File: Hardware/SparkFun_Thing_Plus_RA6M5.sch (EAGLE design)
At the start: 91 parts, among them J1 USB Female Type C Connector, J2 THING_PLUS_LOGICAL, J3 QWIIC_RA, J4 CONN_03X2, J7 MICRO-SDFRICTION, Q2 20V/4.2A/52mΩ/1.4W, U1 R7FA6M5, U2 DA14531MOD, U3 MCP73831, U4 RT9080-33GJ5, U5 W25QXX128MBIT-6X5, U6 MCP1501-3.3V, U7 MAX17048, U8 LM66200, Y1 24.000MHz, Y2 32.768kHz

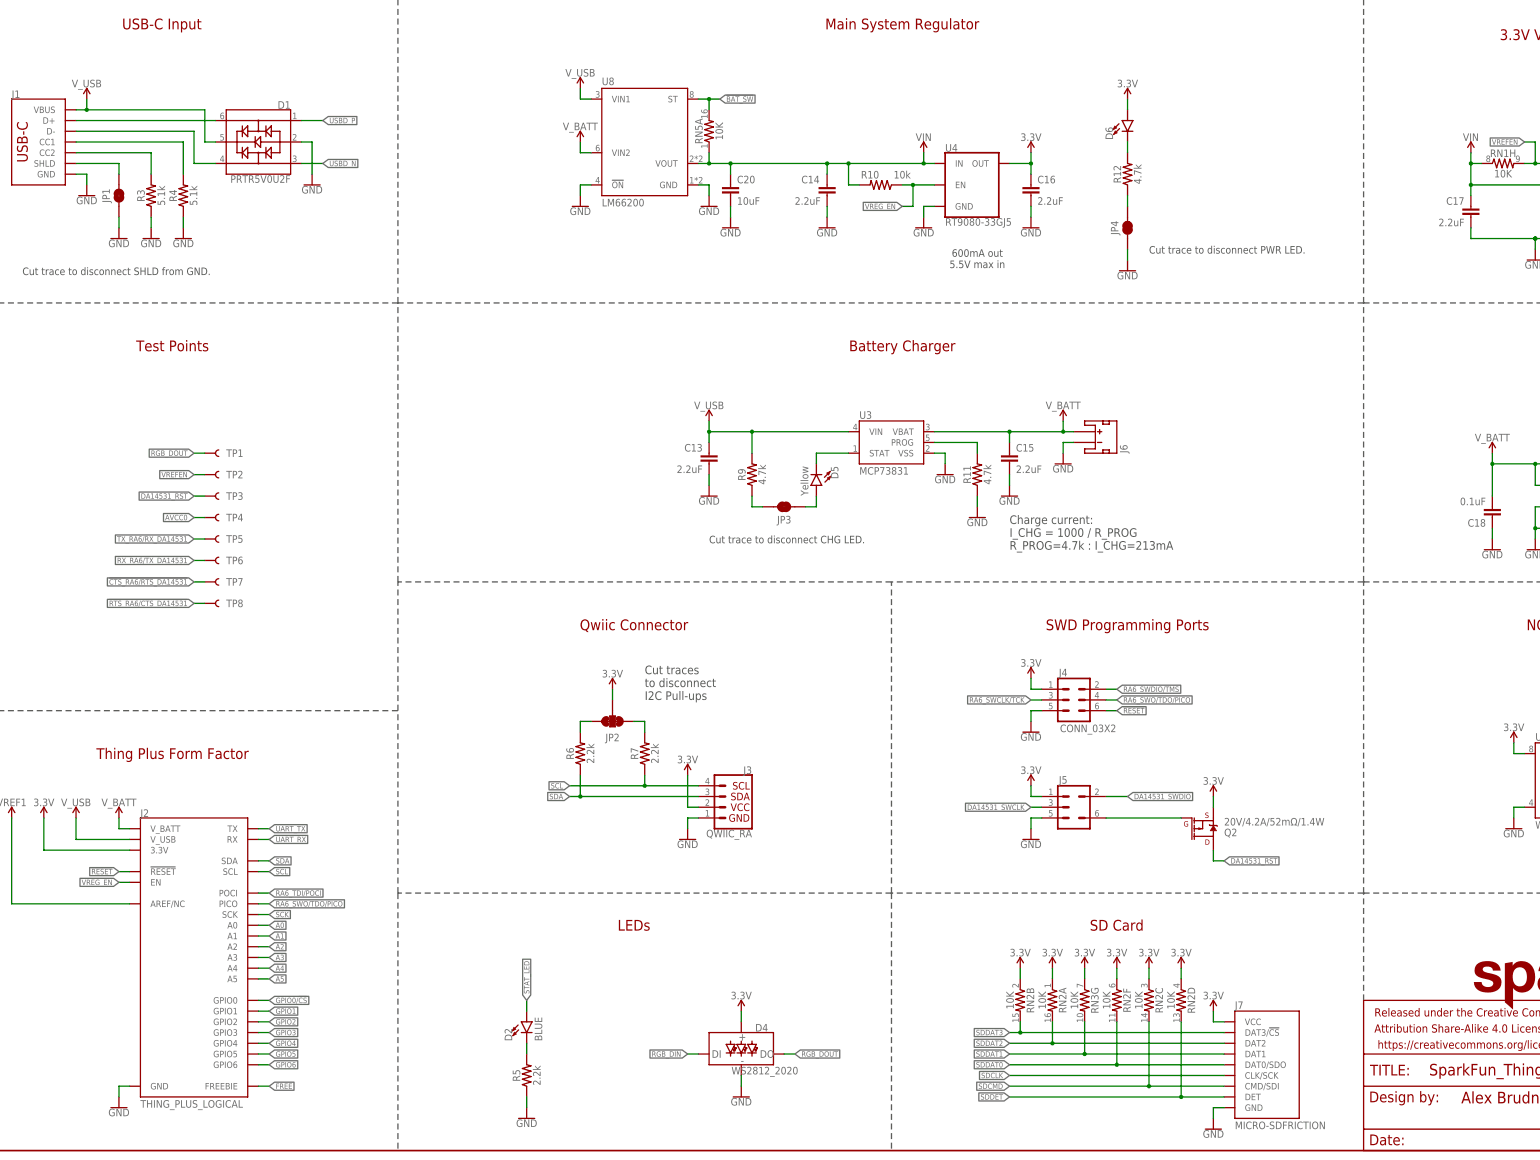
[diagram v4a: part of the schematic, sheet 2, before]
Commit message: update based on pre-design review comments.
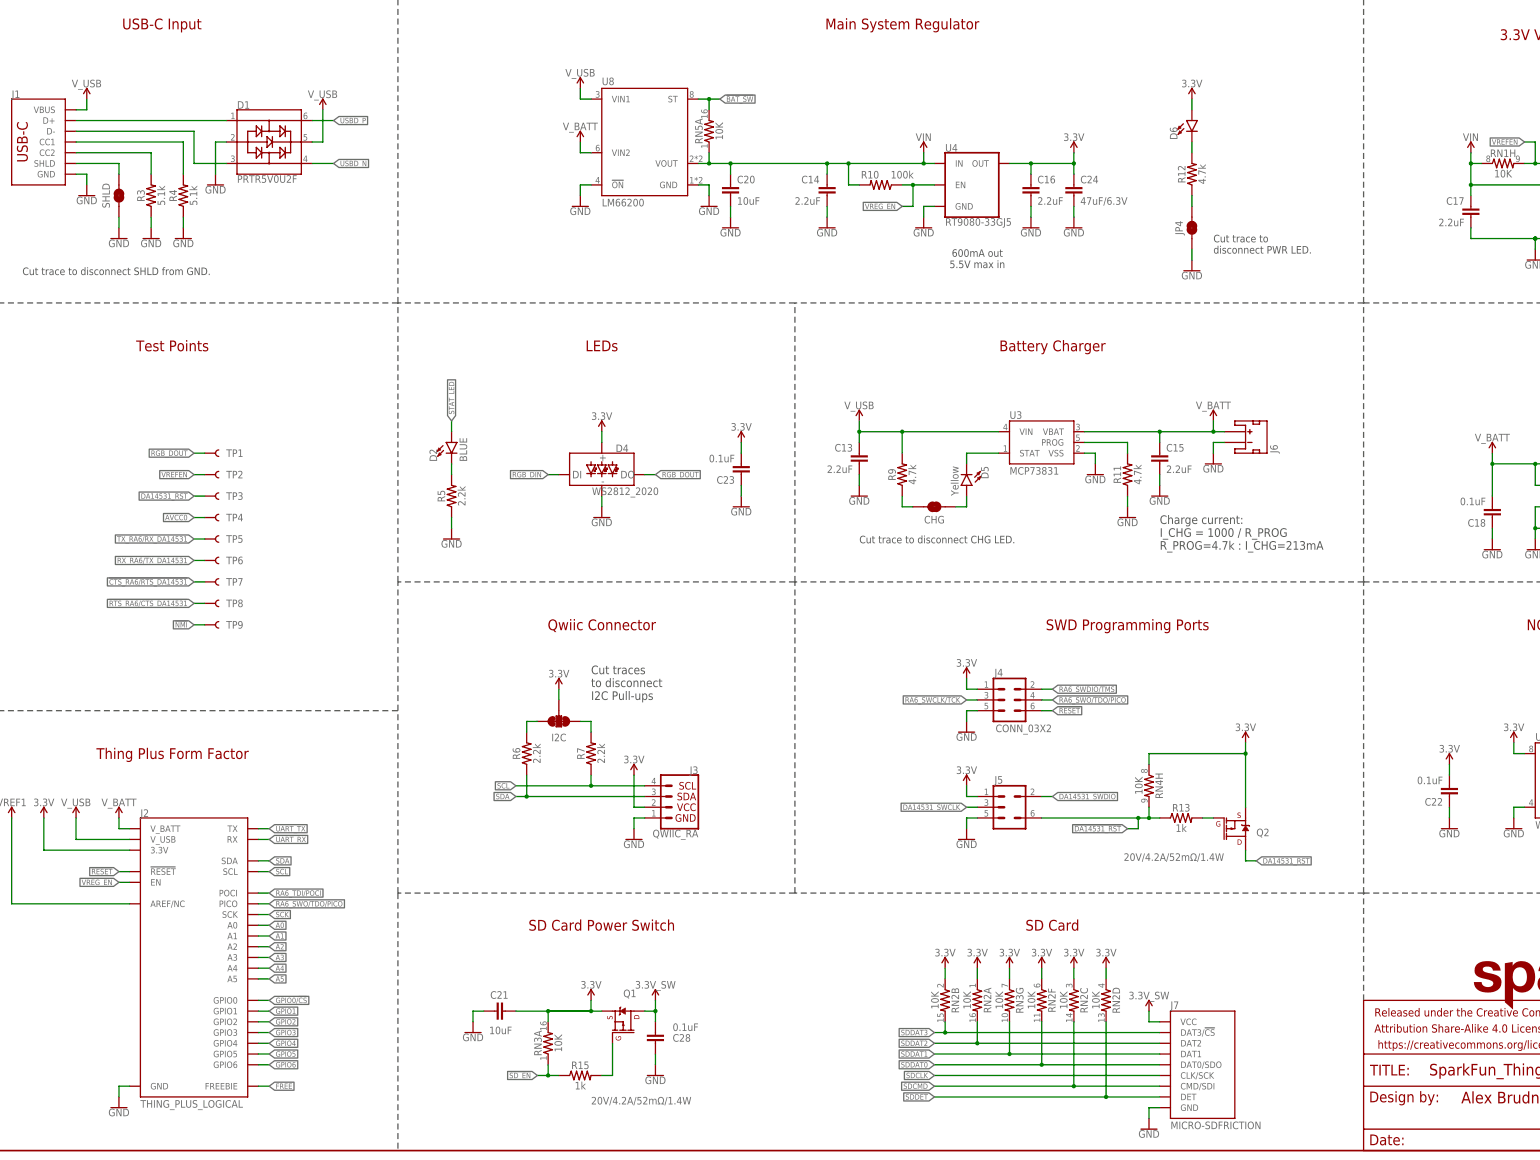
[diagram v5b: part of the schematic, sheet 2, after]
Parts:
- removed JP2: JUMPER-SMT_3_2-NC_TRACE_SILK, SparkFun-Jumpers:JUMPER-SMT_3_2-NC_TRACE_SILK
- removed JP3: JUMPER-SMT_2_NC_TRACE_SILK, SparkFun-Jumpers:JUMPER-SMT_2_NC_TRACE_SILK
- added C21: 10uF, SparkFun-Capacitors:10UF-0805-25V-10%
- added C22, C23, C28: 0.1uF, SparkFun-Capacitors:0.1UF-0402T-16V-10%
- added C24: 47uF/6.3V, SparkFun-Capacitors:47UF
- added C25, C26: 0.1uF, SparkFun-Capacitors:0.1UF-0402T-6.3V-10%-X7R
- added C27: 1.0uF, SparkFun-Capacitors:1.0UF-0402T-16V-10%
- added CHG: JUMPER-SMT_2_NC_TRACE_SILK, SparkFun-Jumpers:JUMPER-SMT_2_NC_TRACE_SILK
- added I2C: JUMPER-SMT_3_2-NC_TRACE_SILK, SparkFun-Jumpers:JUMPER-SMT_3_2-NC_TRACE_SILK
- added Q1: 20V/4.2A/52mΩ/1.4W, SparkFun-DiscreteSemi:MOSFET_PCH-DMG2305UX-7
- added R13, R15: 1k, SparkFun-Resistors:1KOHM-0402T-1/16W-1%
- added TP9: TEST-POINT3, SparkFun-Connectors:TEST-POINT3
- LOGO3: value QWIIC_LOGO_CONNECTOR -> QWIIC_LOGO_4MM; device SparkFun-Aesthetics:QWIIC_LOGO_CONNECTOR -> SparkFun-Aesthetics:QWIIC_LOGO_4MM
- R10: value 10k -> 100k; device SparkFun-Resistors:10KOHM-0402T-1/16W-1% -> SparkFun-Resistors:100KOHM-0402T-1/16W-1%
- renumbered JP1 to SHLD
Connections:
- removed net N$25: RN3B.2, U1G1.P415/USB_VBUSEN/SCL2/SSLB2_B
- removed net N$29: RN4A.2, U1G8.P200/NMI
- removed net N$34: RN4H.2, U1G1.P115/SSITXD0_B/GTIOC4A
- removed net N$8: J5.6, Q2.G
- new net !DA14531_RST!: J5.6, R13.1, RN4H.2, U1G1.P115/SSITXD0_B/GTIOC4A
- new net !NMI!: RN4A.2, TP9.1, U1G8.P200/NMI
- new net !SD_EN!: R15.1, RN3A.1, U1G1.P708/AUDIO_CLK/RXD1/CECIO
- new net 3.3V_SW: C28.2, J7.VCC, Q1.D
- new net N$4: Q2.G, R13.2
- new net N$47: Q1.G, R15.2
- net 3.3V: now also C21.1, C22.2, C23.2, C24.1, I2C.2, Q1.S, RN3A.2, RN3C.2, RN4H.1; no longer J7.VCC, JP2.2, RN3C.1
- net AGND: now also C25.2, C26.2, C27.2
- net AVCC0: now also C25.1
- net GND: now also C21.2, C22.1, C23.1, C24.2, C28.1, RN3B.2; no longer RN3A.1, RN3B.1, RN4H.1
- net N$1: now also CHG.2; no longer JP3.2
- net N$10: now also I2C.1; no longer JP2.1
- net N$11: now also I2C.3; no longer JP2.3
- net N$12: now also RN3C.1; no longer RN3C.2
- net N$13: now also RN3B.1, U1G1.P415/USB_VBUSEN/SCL2/SSLB2_B; no longer RN3A.2, U1G1.P708/AUDIO_CLK/RXD1/CECIO
- net N$17: now also D1.3; no longer D1.4
- net N$2: now also CHG.1; no longer JP3.1
- net N$7: now also D1.1; no longer D1.6
- net USBD_N: now also D1.4; no longer D1.3
- net USBD_P: now also D1.6; no longer D1.1
- net VREF1: now also C26.1, C27.1
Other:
- note added: "SD Card Power Switch"
- moved on the sheet: C13, C15, D1, D2, D4, D5, D6, FB1, J3, J4, J5, J6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

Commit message: Update Sch, Lbr, & Brd files.
Add broken out resistors for boot/reset pins.
Move array resistors around to make them route easier.
Add BAT jumper.
Add 1u to AVCC net.
Move spare array resistor to bottom.
Pull status pin to 3.3V for LM66200.
Make RT9080 PUR 1M.
Replace VREF with another RT9080.
Rename some nets.
Remove SD card PURs since they're available internally on the processor.
Increased the size of some TPs where there was room.
Routed whole board.
Changed thickness of some silk on parts.
Added PROD_IDs to new parts.
Renamed misnamed device.
Delete unused VREF device.
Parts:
- removed RN2: 10K, SparkFun_Thing_Plus_RA6M5:10KOHM-ARRAY(8)-2506_ARV-1/16W-5%
- added BAT, RST: JUMPER-SMT_2_NC_TRACE_SILK, SparkFun-Jumpers:JUMPER-SMT_2_NC_TRACE_SILK
- added C29: 1.0uF, SparkFun-Capacitors:1.0UF-0402T-16V-10%
- added FB2: 120-OHM, SparkFun-Coils:FERRITE_BEAD-120_OHM-0402T
- added R14, R16, R8: 10k, SparkFun-Resistors:10KOHM-0402T-1/16W-1%
- C19: value 1.0nF -> 1.0uF; device SparkFun-Capacitors:1.0NF/1000PF-0402_TIGHT-50V-10% -> SparkFun-Capacitors:1.0UF-0402T-16V-10%
- R10: value 100k -> 1M; device SparkFun-Resistors:100KOHM-0402T-1/16W-1% -> SparkFun-Resistors:1MOHM-0402T-1/16W-5%
- TP1, TP2, TP3, TP5, TP6, TP7, TP8, TP9: value TEST-POINT3 -> TEST-POINT3X4; device SparkFun-Connectors:TEST-POINT3 -> SparkFun-Connectors:TEST-POINT3X4
- U2: device SparkFun_Thing_Plus_RA6M5:DS14531MOD -> SparkFun_Thing_Plus_RA6M5:DA14531MOD
- U6: value MCP1501-3.3V -> RT9080-33GJ5; device SparkFun_Thing_Plus_RA6M5:VREF-3.3V-0.1% -> SparkFun-IC-Power:V_REG_RT9080
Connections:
- net N$105 renamed XCIN
- net N$108 renamed XTAL
- net N$110 renamed XCOUT
- net N$115 renamed EXTAL
- net N$17 renamed USBIN_N
- net N$7 renamed USBIN_P
- removed net !BAT_SW!: RN5A.2, U1G7.P001/AN001/AN101, U8.ST
- removed net !RESET!: J2.!RESET, J4.6, RN2G.2, S2.2, U1G8.!RES!, U2.P0_11
- removed net N$38: RN1F.1, U1G7.P008/AN008
- removed net N$39: RN4B.2, U1G1.P307/CTS6_RTS6/QIO0/GTOUUP_D
- new net !RA6M5_RESET!: J2.!RESET, J4.6, R14.1, S2.2, U1G8.!RES!, U2.P0_11
- new net BAT_SW: RN5B.1, U1G7.P001/AN001/AN101, U8.ST
- new net N$23: RN4B.2, U1G1.P305/TXD6/QSPCLK/GTOWUP
- new net N$25: RST.2, U1G1.P115/SSITXD0_B/GTIOC4A
- new net N$29: C26.1, C27.1, FB2.1, U1G2.VREFH, U1G2.VREFH0
- new net N$7: RN1H.2, U1G7.P008/AN008
- new net N$8: RN3H.2, U1G1.P209/QIO2/SD0WP/GTOVUP
- net !DA14531_RST!: now also R16.2, RST.1; no longer RN4H.2, U1G1.P115/SSITXD0_B/GTIOC4A
- net !FG_ALRT!: now also RN5A.1; no longer RN5B.1
- net !QCS!: now also RN1G.1; no longer RN1G.2
- net !SD_EN!: now also RN3A.2; no longer RN3A.1
- net 3.3V: now also BAT.1, R14.2, R16.1, R8.2, RN1G.2, RN3A.1, RN3C.1, RN5A.2; no longer RN1G.1, RN2A.1, RN2B.1, RN2C.1, RN2D.1, RN2F.1, RN2G.1, RN2H.1, RN3A.2, RN3C.2, RN3G.1, RN4H.1, U1G3.VBATT
- net AGND: now also C29.2
- net AVCC0: now also C29.1
- net BOOT/MD: now also R8.1; no longer RN2H.2
- net GND: now also RN1H.1, RN3B.1, RN3H.1, RN4H.1, RN4H.2; no longer RN1F.2, RN2E.1, RN3B.2
- net N$12: now also RN3B.2, U1G1.P415/USB_VBUSEN/SCL2/SSLB2_B; no longer RN3C.1, U1G1.P414/SDA2/CTS0/SSLB1_B/SD0WP
- net N$13: now also RN3C.2, U1G1.P414/SDA2/CTS0/SSLB1_B/SD0WP; no longer RN3B.1, U1G1.P415/USB_VBUSEN/SCL2/SSLB2_B
- net N$15: now also RN3G.2; no longer RN3H.2
- net N$30: now also U1G1.P307/CTS6_RTS6/QIO0/GTOUUP_D; no longer U1G1.P305/TXD6/QSPCLK/GTOWUP
- net N$33: now also BAT.2, U1G3.VBATT; no longer RN2E.2, U1G1.P209/QIO2/SD0WP/GTOVUP
- net N$9: now also RN3G.1; no longer RN3H.1
- net SDCMD: no longer RN2C.2
- net SDDAT0: no longer RN2F.2
- net SDDAT1: no longer RN3G.2
- net SDDAT2: no longer RN2A.2
- net SDDAT3: no longer RN2B.2
- net SDDET: no longer RN2D.2
- net VIN: now also RN1F.2, U6.IN; no longer RN1H.1, RN5A.1, U6.VDD
- net VREF1: now also FB2.2; no longer C26.1, C27.1, U1G2.VREFH, U1G2.VREFH0
- net VREFEN: now also RN1F.1, U6.EN; no longer RN1H.2, U6.!SHDN!
- net V_BATT: now also U8.VIN1; no longer U8.VIN2
- net V_USB: now also U8.VIN2; no longer U8.VIN1
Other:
- note added: "Cut BAT trace to supply your own battery."
- note added: "Cut RST trace to remove BLE module reset capability. In case doing this causes a boot loop. To be removed or disabled in reds."
- note added: "Extra 10k in array."
- moved on the sheet: C26, C27, FB1, J7, RN1G, RN3A, RN3B, RN3C, RN3H, RN4B, RN4D, RN5A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
